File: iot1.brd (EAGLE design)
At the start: 95 x 100 mm, 77 parts, among them IC1 OPA2134PA, IC2 MEGA8-P, IC3 4051N, IC4 7805T, IC5 7805T, IC6 MAX3468CPA, IC7 LTC2486C, J1 DCJ0202, Q1 16MHz, U1 HTU21D, U2 LM2577T-ADJ/NOPB, X1 A1944-50, X2 22-23-2041, X3 22-23-2041, X4 22-23-2041

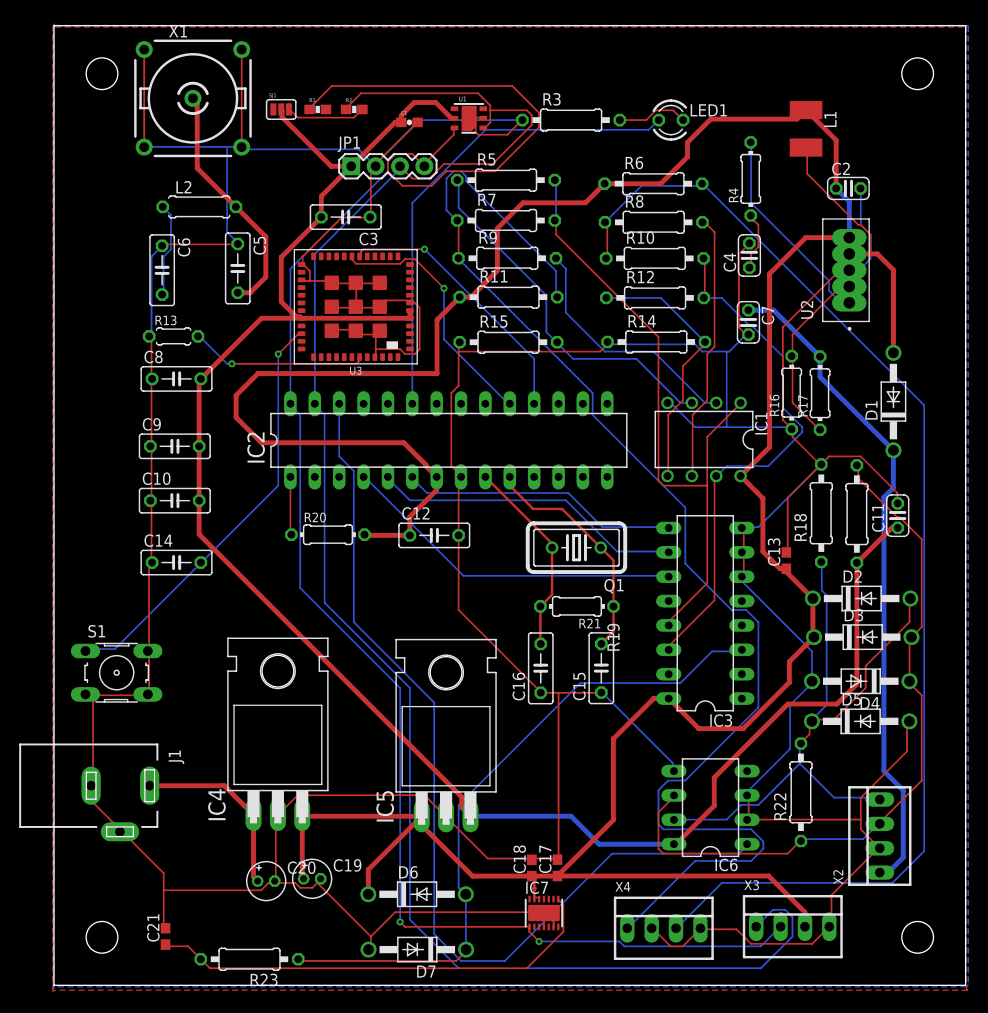
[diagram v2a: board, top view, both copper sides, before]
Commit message: fixing wiring errors
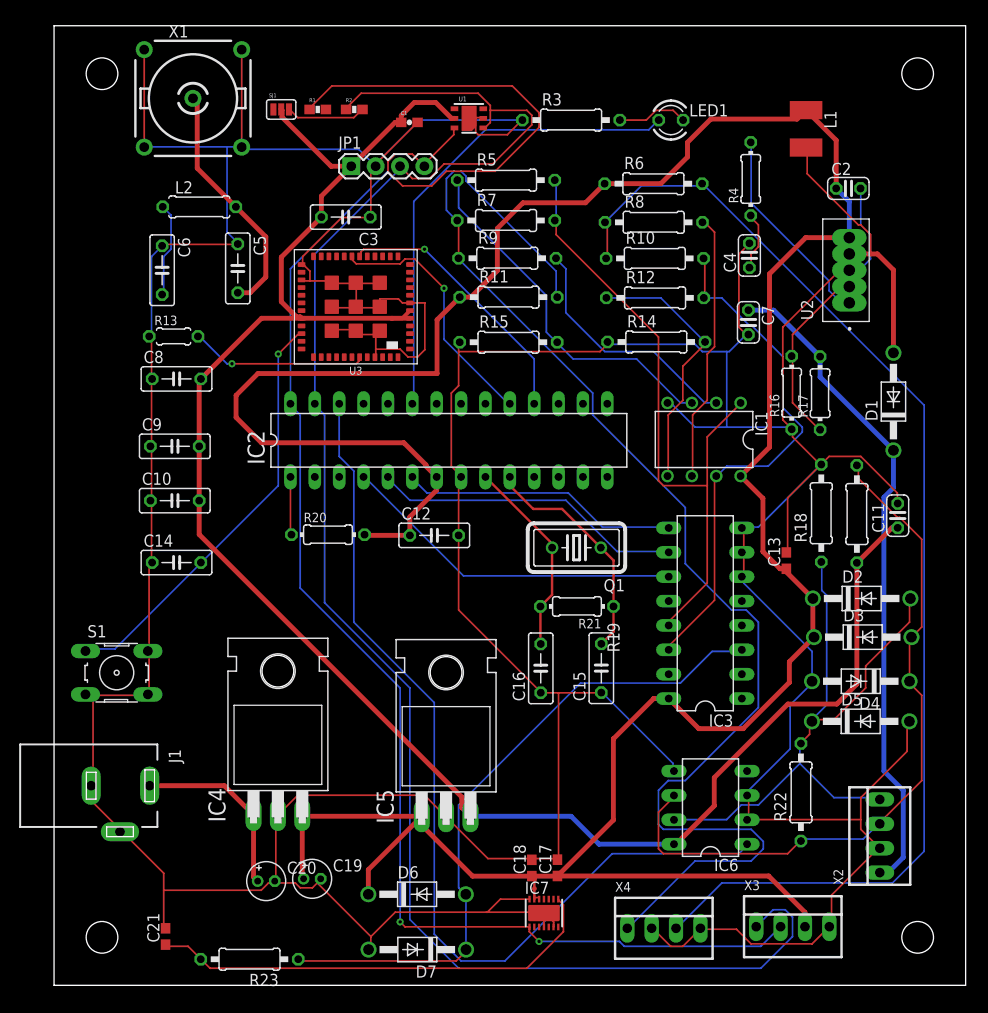
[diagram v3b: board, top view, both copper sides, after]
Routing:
- net GND: track 631.6 -> 639.0 mm
- net 3.3V: track 195.8 -> 197.2 mm
- removed copper zone on layer 1, net GND
- removed copper zone on layer 16, net GND
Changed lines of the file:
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@@
 <grid distance="0.5" unitdist="mil" unit="mm" style="lines" multiple="1" display="yes" altdistance="0.5" altunitdist="mil" altunit="mm"/>
 <layers>
-<layer number="1" name="Top" color="4" fill="1" visible="no" active="yes"/>
+<layer number="1" name="Top" color="4" fill="1" visible="yes" active="yes"/>
 <layer number="2" name="Route2" color="16" fill="1" visible="no" active="no"/>
 <layer number="3" name="Route3" color="17" fill="1" visible="no" active="no"/>
@@
 <layer number="14" name="Route14" color="22" fill="1" visible="no" active="no"/>
 <layer number="15" name="Route15" color="23" fill="1" visible="no" active="no"/>
-<layer number="16" name="Bottom" color="1" fill="1" visible="no" active="yes"/>
-<layer number="17" name="Pads" color="2" fill="1" visible="no" active="yes"/>
-<layer number="18" name="Vias" color="2" fill="1" visible="no" active="yes"/>
-<layer number="19" name="Unrouted" color="6" fill="1" visible="no" active="yes"/>
+<layer number="16" name="Bottom" color="1" fill="1" visible="yes" active="yes"/>
+<layer number="17" name="Pads" color="2" fill="1" visible="yes" active="yes"/>
+<layer number="18" name="Vias" color="2" fill="1" visible="yes" active="yes"/>
+<layer number="19" name="Unrouted" color="6" fill="1" visible="yes" active="yes"/>
 <layer number="20" name="Dimension" color="24" fill="1" visible="yes" active="yes"/>
 <layer number="21" name="tPlace" color="7" fill="1" visible="yes" active="yes"/>
@@
 <autorouter>
 <pass name="Default">
-<param name="RoutingGrid" value="50mil"/>
+<param name="RoutingGrid" value="0.5mm"/>
 <param name="AutoGrid" value="1"/>
 <param name="Efforts" value="2"/>
 <param name="TopRouterVariant" value="1"/>
 <param name="tpViaShape" value="round"/>
-<param name="PrefDir.1" value="a"/>
+<param name="PrefDir.1" value="|"/>
 <param name="PrefDir.2" value="0"/>
 <param name="PrefDir.3" value="0"/>
@@
 <param name="PrefDir.14" value="0"/>
 <param name="PrefDir.15" value="0"/>
-<param name="PrefDir.16" value="a"/>
+<param name="PrefDir.16" value="*"/>
 <param name="cfVia" value="8"/>
 <param name="cfNonPref" value="5"/>
@@
 <wire x1="52.07" y1="6.096" x2="52.054" y2="6.0811" width="0.1778" layer="1"/>
 <wire x1="51.054" y1="7.366" x2="51.054" y2="7.5311" width="0.1778" layer="1"/>
-<wire x1="35.56" y1="7.62" x2="51.054" y2="7.62" width="0.1778" layer="1"/>
+<wire x1="35.56" y1="7.62" x2="45.0596" y2="7.62" width="0.1778" layer="1"/>
+<wire x1="45.0596" y1="7.62" x2="45.1612" y2="7.62" width="0.1778" layer="1"/>
+<wire x1="45.1612" y1="7.62" x2="51.054" y2="7.62" width="0.1778" layer="1"/>
 <wire x1="33.02" y1="5.08" x2="35.56" y2="7.62" width="0.1778" layer="1"/>
 <wire x1="33.02" y1="3.81" x2="33.02" y2="5.08" width="0.1778" layer="1"/>
@@
 <wire x1="31.242" y1="73.152" x2="31.4452" y2="73.2136" width="0.1778" layer="1"/>
 <wire x1="36.068" y1="66.294" x2="33.528" y2="66.294" width="0.1778" layer="1"/>
-<wire x1="36.576" y1="65.786" x2="36.068" y2="66.294" width="0.1778" layer="1"/>
-<wire x1="37.592" y1="65.786" x2="36.576" y2="65.786" width="0.1778" layer="1"/>
-<wire x1="38.1" y1="66.294" x2="37.592" y2="65.786" width="0.1778" layer="1"/>
-<wire x1="38.1" y1="70.612" x2="38.1" y2="66.294" width="0.1778" layer="1"/>
-<wire x1="37.338" y1="71.374" x2="38.1" y2="70.612" width="0.1778" layer="1"/>
-<wire x1="34.544" y1="71.374" x2="37.338" y2="71.374" width="0.1778" layer="1"/>
-<wire x1="34.036" y1="70.866" x2="34.544" y2="71.374" width="0.1778" layer="1"/>
+<wire x1="36.8808" y1="65.4812" x2="36.068" y2="66.294" width="0.1778" layer="1"/>
+<wire x1="37.887440625" y1="65.4812" x2="36.8808" y2="65.4812" width="0.1778" layer="1"/>
+<wire x1="38.6461" y1="66.239859375" x2="37.887440625" y2="65.4812" width="0.1778" layer="1"/>
 <wire x1="34.036" y1="70.866" x2="33.9452" y2="70.7136" width="0.1778" layer="1"/>
 <wire x1="43.18" y1="90.424" x2="43.942" y2="90.424" width="0.1778" layer="1"/>
@@
 <wire x1="50.546" y1="30.734" x2="42.164" y2="39.116" width="0.1778" layer="1"/>
 <wire x1="50.546" y1="30.734" x2="50.7238" y2="30.4927" width="0.1778" layer="1"/>
-<polygon width="0.508" layer="1">
-<vertex x="0.127" y="99.8728"/>
-<vertex x="94.9579" y="99.8728"/>
-<vertex x="95.0976" y="100.0125"/>
-<vertex x="95.0976" y="-0.381"/>
-<vertex x="95.2246" y="-0.508"/>
-<vertex x="0" y="-0.508"/>
-<vertex x="-0.127" y="-0.635"/>
-<vertex x="-0.127" y="99.822"/>
-<vertex x="-0.0381" y="99.9109"/>
-<vertex x="0.0889" y="99.9109"/>
-</polygon>
-<polygon width="0.508" layer="16">
-<vertex x="0.0635" y="100.0252"/>
-<vertex x="95.2373" y="100.0252"/>
-<vertex x="95.2881" y="99.9744"/>
-<vertex x="95.2881" y="0.0635"/>
-<vertex x="95.0722" y="-0.1524"/>
-<vertex x="0.0889" y="-0.1524"/>
-<vertex x="-0.0635" y="-0.3048"/>
-<vertex x="-0.0635" y="100.0633"/>
-<vertex x="0.0635" y="100.1903"/>
-</polygon>
-<wire x1="33.9452" y1="70.7136" x2="37.0952" y2="71.1136" width="0" layer="19" extent="1-1"/>
-<wire x1="49.554" y1="8.9811" x2="51.054" y2="7.5311" width="0" layer="19" extent="1-1"/>
+<wire x1="38.6461" y1="71.1136" x2="37.0952" y2="71.1136" width="0.1778" layer="1"/>
+<wire x1="38.6461" y1="71.1136" x2="38.6461" y2="66.239859375" width="0.1778" layer="1"/>
+<wire x1="33.9452" y1="70.7136" x2="33.9452" y2="71.5327" width="0.1778" layer="1"/>
+<wire x1="35.8887" y1="71.5327" x2="33.9452" y2="71.5327" width="0.1778" layer="1"/>
+<wire x1="36.3078" y1="71.1136" x2="37.0952" y2="71.1136" width="0.1778" layer="1"/>
+<wire x1="36.3078" y1="71.1136" x2="35.8887" y2="71.5327" width="0.1778" layer="1"/>
+<wire x1="49.554" y1="8.9811" x2="46.5223" y2="8.9811" width="0.1778" layer="1"/>
+<wire x1="46.5223" y1="8.9811" x2="45.1612" y2="7.62" width="0.1778" layer="1"/>
 </signal>
 <signal name="SCL">
@@
 <via x="50.546" y="4.572" extent="1-16" drill="0.35"/>
 <via x="36.068" y="6.604" extent="1-16" drill="0.35"/>
-<wire x1="49.554" y1="6.0811" x2="50.554" y2="6.0811" width="0" layer="19" extent="1-1"/>
 </signal>
 <signal name="SDA">
@@
 <wire x1="37.338" y1="84.074" x2="39.116" y2="84.074" width="0.1778" layer="1"/>
 <wire x1="36.0553" y1="85.3567" x2="37.338" y2="84.074" width="0.1778" layer="1"/>
-<wire x1="73.1774" y1="6.1087" x2="50.054" y2="6.0811" width="0" layer="19" extent="1-1"/>
 </signal>
 <signal name="3.3V">
@@
 <wire x1="15.3035" y1="63.1952" x2="21.6219" y2="69.5136" width="0.508" layer="1"/>
 <wire x1="21.6219" y1="69.5136" x2="25.7952" y2="69.5136" width="0.508" layer="1"/>
-<wire x1="25.7952" y1="69.5136" x2="37.0952" y2="69.5136" width="0.508" layer="1"/>
-<wire x1="37.0952" y1="69.5136" x2="37.0952" y2="70.3136" width="0.508" layer="1"/>
+<wire x1="25.7952" y1="69.5136" x2="35.2171" y2="69.5136" width="0.508" layer="1"/>
+<wire x1="35.2171" y1="69.5136" x2="37.0952" y2="69.5136" width="0.508" layer="1"/>
 <wire x1="23.7617" y1="90.4715625" x2="23.7617" y2="91.186" width="0.508" layer="1"/>
 <wire x1="23.7617" y1="91.186" x2="23.6728" y2="91.2749" width="0.508" layer="1"/>
@@
 <wire x1="23.6855" y1="75.8825" x2="27.8638" y2="80.0608" width="0.508" layer="1"/>
 <wire x1="23.6855" y1="71.2425" x2="23.6855" y2="75.8825" width="0.508" layer="1"/>
+<wire x1="37.0952" y1="70.3136" x2="36.2952" y2="69.5136" width="0.4064" layer="1"/>
+<wire x1="36.2952" y1="69.5136" x2="35.2171" y2="69.5136" width="0.4064" layer="1"/>
 </signal>
 <signal name="N$13">
@@
 <wire x1="24.638" y1="91.186" x2="25.4" y2="90.424" width="0.1778" layer="1"/>
 <wire x1="32.004" y1="91.186" x2="32.1428" y2="91.2749" width="0.1778" layer="1"/>
-<wire x1="24.638" y1="91.186" x2="24.4856" y2="91.2749" width="0" layer="19" extent="1-1"/>
 </signal>
 <signal name="N$14">
 <contactref element="R1" pad="2"/>
 <contactref element="SJ1" pad="1"/>
-<wire x1="22.86" y1="91.2749" x2="28.3328" y2="91.2749" width="0" layer="19" extent="1-1"/>
 </signal>
 <signal name="N$15">
 <contactref element="IC2" pad="23"/>
 <contactref element="LED1" pad="A"/>
-<wire x1="37.338" y1="81.534" x2="37.338" y2="60.6044" width="0.1778" layer="16"/>
-<wire x1="44.958" y1="89.154" x2="37.338" y2="81.534" width="0.1778" layer="16"/>
+<wire x1="37.4904" y1="81.6864" x2="37.4904" y2="60.7568" width="0.1778" layer="16"/>
+<wire x1="37.4904" y1="60.7568" x2="37.338" y2="60.6044" width="0.1778" layer="16"/>
+<wire x1="44.958" y1="89.154" x2="37.4904" y2="81.6864" width="0.1778" layer="16"/>
 <wire x1="61.976" y1="89.154" x2="44.958" y2="89.154" width="0.1778" layer="16"/>
 <wire x1="62.992" y1="90.17" x2="61.976" y2="89.154" width="0.1778" layer="16"/>
@@
 <wire x1="11.3284" y1="81.1276" x2="12.192" y2="80.264" width="0.1778" layer="16"/>
 <wire x1="11.43" y1="72.136" x2="11.2649" y2="71.9836" width="0.1778" layer="16"/>
-<wire x1="11.2649" y1="71.9836" x2="25.7952" y2="74.3136" width="0" layer="19" extent="1-1"/>
 </signal>
 <signal name="N$6">

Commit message: fixing wiring errors
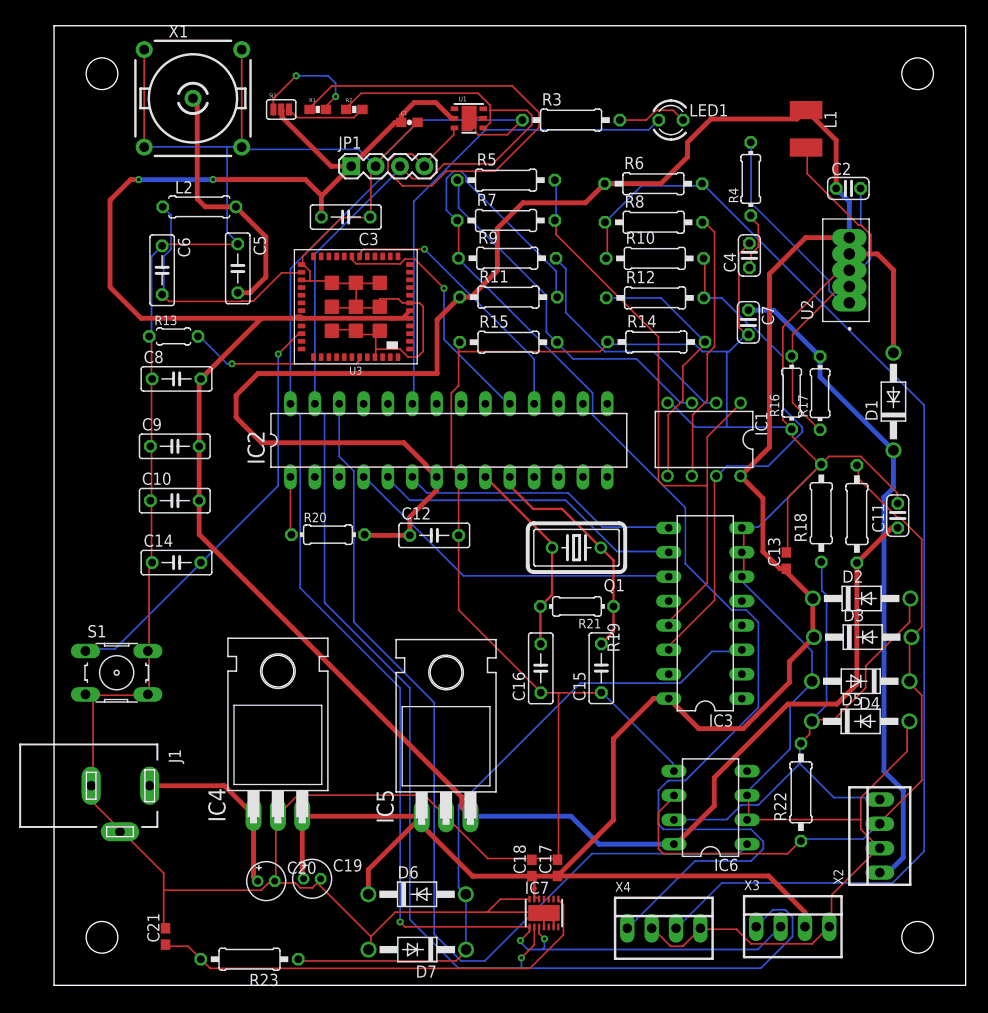
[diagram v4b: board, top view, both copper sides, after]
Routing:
- net 3.3V: track 197.2 -> 234.3 mm, vias 0 -> 2
- net N$30: track 9.89 -> 26.0 mm
- net N$14: track 0.00 -> 12.1 mm, vias 0 -> 2
- net SCL: track 192.2 -> 197.1 mm, vias 2 -> 3
- net SDA: track 177.8 -> 182.7 mm, vias 0 -> 1
- net RF_LORAWAN: track 25.4 -> 27.2 mm
